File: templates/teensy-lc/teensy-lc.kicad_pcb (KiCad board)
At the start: 2 copper layers, 1 part, among them J1 TEENSY LC

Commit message: Moved wickerbox templates out. Teensy is messed up.
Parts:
- J1: value TEENSY LC -> TEENSY-LC; footprint TEENSY-LC -> Wickerlib:TEENSY-LC
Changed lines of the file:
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@@
-(kicad_pcb (version 4) (host pcbnew 4.0.4+e1-6308~48~ubuntu14.04.1-stable)
+(kicad_pcb (version 4) (host pcbnew 4.0.5-e0-6337~49~ubuntu16.04.1)
   (general
     (links 3)
     (no_connects 3)
-    (area 90.094999 71.043799 178.510001 123.265001)
+    (area 0 0 0 0)
     (thickness 1.6)
     (drawings 21)
@@
   (page USLetter)
   (title_block
+    (title "Project Title")
+    (rev v1.0)
     (company "Released under the CERN Open Hardware License v1.2")
-    (comment 1 "jenner@wickerbox.net - http://wickerbox.net")
-    (comment 2 "Designed by Jenner at Wickerbox Electronics")
+    (comment 1 "Based on template by jenner@wickerbox.net")
   )
   (layers
@@
     (add_net GND)
   )
-  (module TEENSY-LC (layer F.Cu)
+  (module Wickerlib:TEENSY-LC (layer F.Cu)
     (at 105.41 82.804)
     (fp_text reference J1 (at -7.62 20.066 270) (layer F.SilkS)
       (effects (font (size 1 1) (thickness 0.15)))
     )
-    (fp_text value "TEENSY LC" (at -2.54 20.32 180) (layer F.Fab)
+    (fp_text value TEENSY-LC (at -2.54 20.32 180) (layer F.Fab)
       (effects (font (size 1 1) (thickness 0.15)))
     )
@@
       (effects (font (size 1 1) (thickness 0.15)) (justify mirror))
     )
-    (fp_line (start -11.43 24.13) (end 6.35 24.13) (layer F.CrtYd) (width 0.1524))
-    (fp_line (start -11.43 -11.43) (end -11.43 24.13) (layer F.CrtYd) (width 0.1524))
-    (fp_line (start 6.35 -11.43) (end -11.43 -11.43) (layer F.CrtYd) (width 0.1524))
-    (fp_line (start 6.35 24.13) (end 6.35 -11.43) (layer F.CrtYd) (width 0.1524))
+    (fp_line (start -11.43 24.13) (end 6.35 24.13) (layer F.Fab) (width 0.1524))
+    (fp_line (start -11.43 -11.43) (end -11.43 24.13) (layer F.Fab) (width 0.1524))
+    (fp_line (start 6.35 -11.43) (end -11.43 -11.43) (layer F.Fab) (width 0.1524))
+    (fp_line (start 6.35 24.13) (end 6.35 -11.43) (layer F.Fab) (width 0.1524))
     (pad G1 thru_hole circle (at -10.16 -10.16) (size 1.7272 1.7272) (drill 1.016) (layers *.Cu *.Mask F.SilkS)
       (net 1 GND))

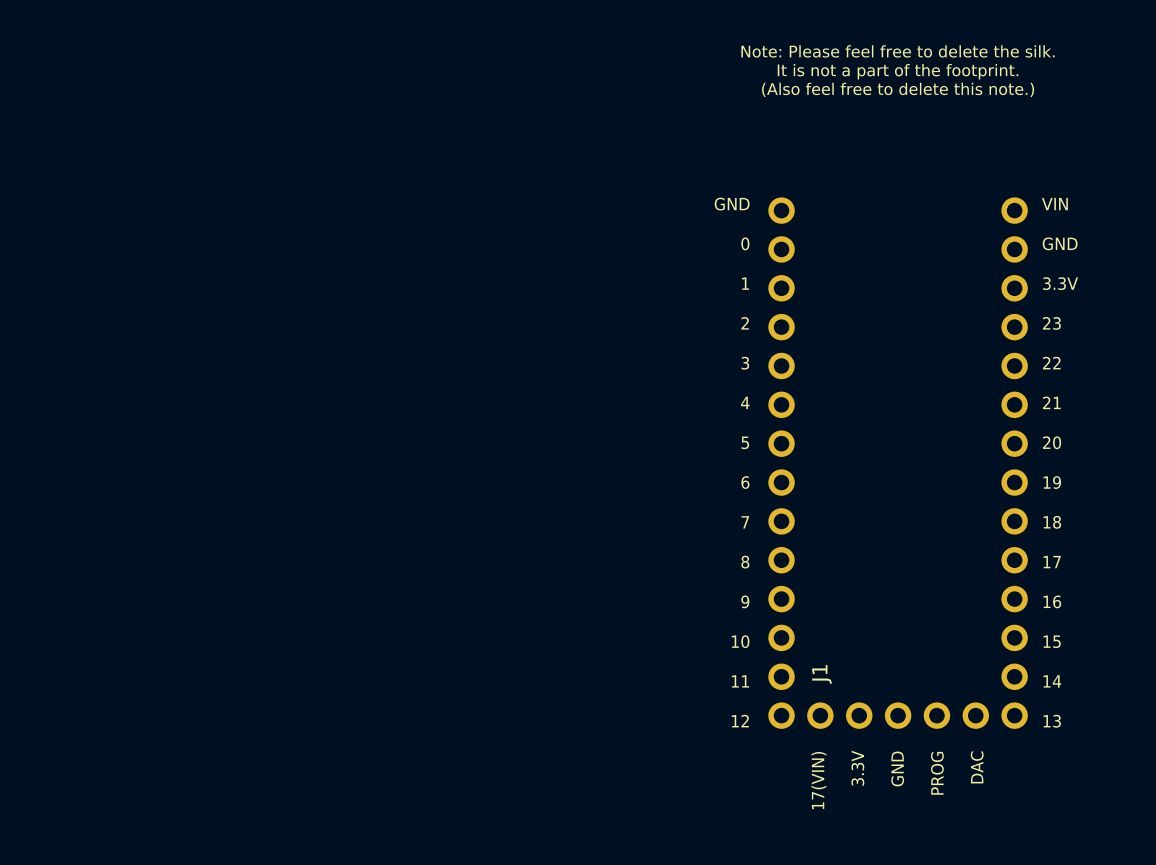
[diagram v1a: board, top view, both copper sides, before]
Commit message: Add fab notes to Dwgs.User
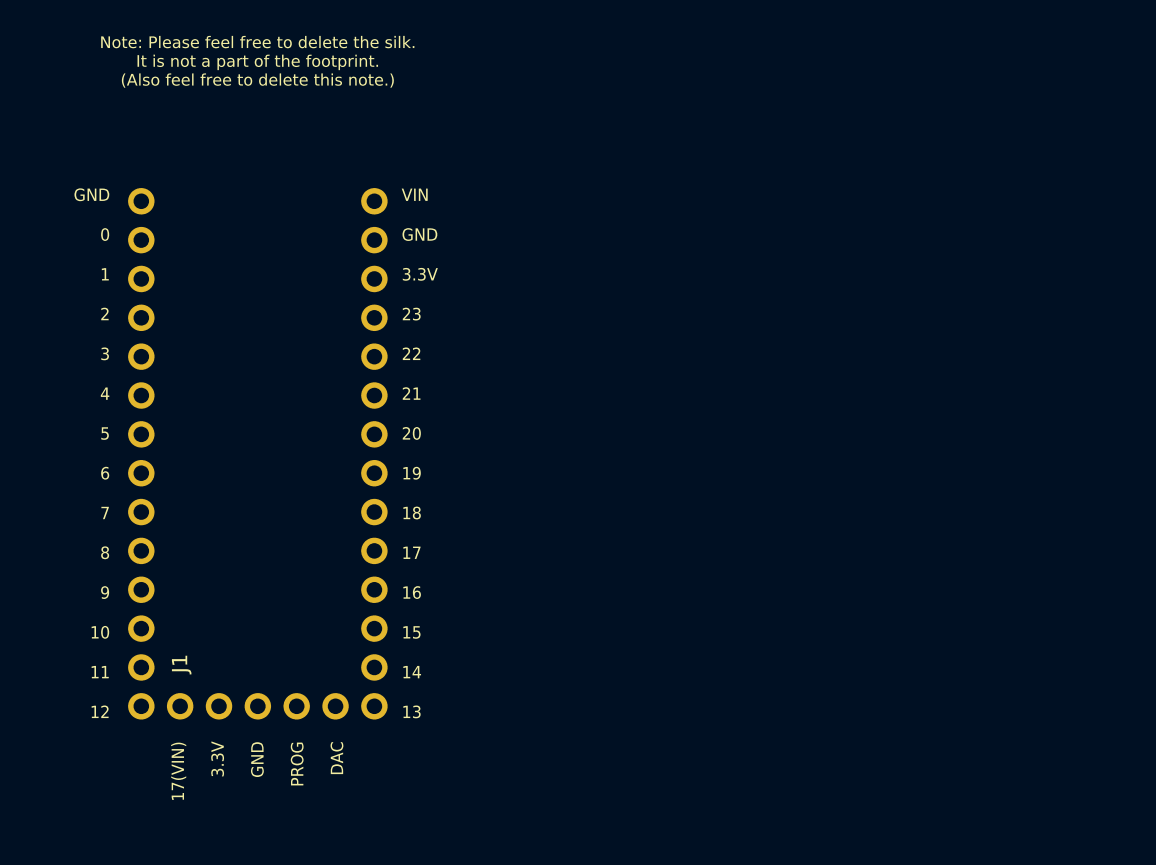
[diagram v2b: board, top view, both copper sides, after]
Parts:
- moved J1 41.9 mm to (63.6, 82.2)
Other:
- board text added: "FABRICATION NOTES 1. THIS IS A 2 LAYER BOARD. 2. EXTERNAL LAYERS SHALL HAVE 1 OZ COPPER. 3. MATERIAL: FR4 AND 0.062 INCH +/- 10% THICK. 4. BOARDS SHALL BE ROHS COMPLIANT. 5. MANUFACTURE IN ACCORDANCE WITH IPC-6012 CLASS 2 6. MASK: BOTH SIDES OF THE BOARD SHALL HAVE SOLDER MASK (ANY COLOR) OVER BARE COPPER. 7. SILK: BOTH SIDES OF THE BOARD SHALL HAVE WHITE SILKSCREEN. DO NOT PLACE SILK OVER BARE C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"
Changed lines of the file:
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@@
-(kicad_pcb (version 4) (host pcbnew 4.0.5-e0-6337~49~ubuntu16.04.1)
+(kicad_pcb (version 4) (host pcbnew 4.0.7-e2-6376~58~ubuntu16.04.1)
   (general
     (links 3)
     (no_connects 3)
-    (area 0 0 0 0)
+    (area 90.895714 61.595 178.510001 123.265001)
     (thickness 1.6)
-    (drawings 21)
+    (drawings 5)
     (tracks 0)
     (zones 0)
@@
     (38 B.Mask user)
     (39 F.Mask user)
+    (40 Dwgs.User user)
     (44 Edge.Cuts user)
     (46 B.CrtYd user)
@@
   )
   (module Wickerlib:TEENSY-LC (layer F.Cu)
-    (at 105.41 82.804)
+    (at 63.5508 82.1944)
     (fp_text reference J1 (at -7.62 20.066 270) (layer F.SilkS)
       (effects (font (size 1 1) (thickness 0.15)))
@@
     (pad 15 thru_hole circle (at 5.08 17.78) (size 1.7272 1.7272) (drill 1.016) (layers *.Cu *.Mask F.SilkS))
   )
-  (gr_text "Note: Please feel free to delete the silk.\nIt is not a part of the footprint.\n(Also feel free to delete this note.)" (at 102.87 63.5) (layer F.SilkS)
+  (gr_text "FABRICATION NOTES\n\n1. THIS IS A 2 LAYER BOARD. \n2. EXTERNAL LAYERS SHALL HAVE 1 OZ COPPER.\n3. MATERIAL: FR4 AND 0.062 INCH +/- 10% THICK.\n4. BOARDS SHALL BE ROHS COMPLIANT. \n5. MANUFACTURE IN ACCORDANCE WITH IPC-6012 CLASS 2\n6. MASK: BOTH SIDES OF THE BOARD SHALL HAVE \n   SOLDER MASK (ANY COLOR) OVER BARE COPPER. \n7. SILK: BOTH SIDES OF THE BOARD SHALL HAVE \n   WHITE SILKSCREEN. DO NOT PLACE SILK OVER BARE COPPER.\n8. FINISH: ENIG.\n9. MINIMUM TRACE WIDTH - 0.006 INCH.\n   MINIMUM SPACE - 0.006 INCH.\n   MINIMUM HOLE DIA - 0.013 INCH. \n10. MAX HOLE PLACEMENT TOLERANCE OF +/- 0.003 INCH.\n11. MAX HOLE DIAMETER TOLERANCE OF +/- 0.003 INCH AFTER PLATING." (at 108.1532 87.63) (layer Dwgs.User)
+    (effects (font (size 2.54 2.54) (thickness 0.254)) (justify left))
+  )
+  (gr_text "Note: Please feel free to delete the silk.\nIt is not a part of the footprint.\n(Also feel free to delete this note.)" (at 61.0108 62.8904) (layer F.SilkS)
     (effects (font (size 0.762 0.762) (thickness 0.1524)))
   )
-  (gr_text "VIN\n\nGND\n\n3.3V\n\n23\n\n22\n\n21\n\n20\n\n19\n\n18\n\n17\n\n16\n\n15\n\n14\n\n13\n" (at 112.268 89.154) (layer F.SilkS)
+  (gr_text "VIN\n\nGND\n\n3.3V\n\n23\n\n22\n\n21\n\n20\n\n19\n\n18\n\n17\n\n16\n\n15\n\n14\n\n13\n" (at 70.4088 88.5444) (layer F.SilkS)
     (effects (font (size 0.80772 0.762) (thickness 0.1524)) (justify left))
   )
-  (gr_text "GND\n\n0\n\n1\n\n2\n\n3\n\n4\n\n5\n\n6\n\n7\n\n8\n\n9\n\n10\n\n11\n\n12" (at 93.218 89.154) (layer F.SilkS)
+  (gr_text "GND\n\n0\n\n1\n\n2\n\n3\n\n4\n\n5\n\n6\n\n7\n\n8\n\n9\n\n10\n\n11\n\n12" (at 51.3588 88.5444) (layer F.SilkS)
     (effects (font (size 0.80772 0.762) (thickness 0.1524)) (justify right))
   )
-  (gr_text "17(VIN)\n\n3.3V\n\nGND\n\nPROG\n\nDAC" (at 102.87 107.95 90) (layer F.SilkS)
+  (gr_text "17(VIN)\n\n3.3V\n\nGND\n\nPROG\n\nDAC" (at 61.0108 107.3404 90) (layer F.SilkS)
     (effects (font (size 0.80772 0.762) (thickness 0.1524)) (justify right))
   )
-  (gr_circle (center 117.348 76.962) (end 118.618 76.962) (layer Dwgs.User) (width 0.15))
-  (gr_line (start 114.427 78.994) (end 114.427 74.93) (angle 90) (layer Dwgs.User) (width 0.15))
-  (gr_line (start 120.269 78.994) (end 114.427 78.994) (angle 90) (layer Dwgs.User) (width 0.15))
-  (gr_line (start 120.269 74.93) (end 120.269 78.994) (angle 90) (layer Dwgs.User) (width 0.15))
-  (gr_line (start 114.427 74.93) (end 120.269 74.93) (angle 90) (layer Dwgs.User) (width 0.15))
-  (gr_line (start 120.523 93.98) (end 104.648 93.98) (angle 90) (layer Dwgs.User) (width 0.15))
-  (gr_line (start 173.355 102.235) (end 173.355 94.615) (angle 90) (layer Dwgs.User) (width 0.15))
-  (gr_line (start 178.435 102.235) (end 173.355 102.235) (angle 90) (layer Dwgs.User) (width 0.15))
-  (gr_line (start 178.435 94.615) (end 178.435 102.235) (angle 90) (layer Dwgs.User) (width 0.15))
-  (gr_line (start 173.355 94.615) (end 178.435 94.615) (angle 90) (layer Dwgs.User) (width 0.15))
-  (gr_line (start 109.093 123.19) (end 109.093 114.3) (angle 90) (layer Dwgs.User) (width 0.15))
-  (gr_line (start 122.428 123.19) (end 109.093 123.19) (angle 90) (layer Dwgs.User) (width 0.15))
-  (gr_line (start 122.428 114.3) (end 122.428 123.19) (angle 90) (layer Dwgs.User) (width 0.15))
-  (gr_line (start 109.093 114.3) (end 122.428 114.3) (angle 90) (layer Dwgs.User) (width 0.15))
-  (gr_line (start 104.648 93.98) (end 104.648 82.55) (angle 90) (layer Dwgs.User) (width 0.15))
-  (gr_line (start 120.523 82.55) (end 120.523 93.98) (angle 90) (layer Dwgs.User) (width 0.15))
-  (gr_line (start 104.648 82.55) (end 120.523 82.55) (angle 90) (layer Dwgs.User) (width 0.15))
 )
